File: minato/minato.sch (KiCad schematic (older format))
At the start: 211 parts, among them U1 Elite-C

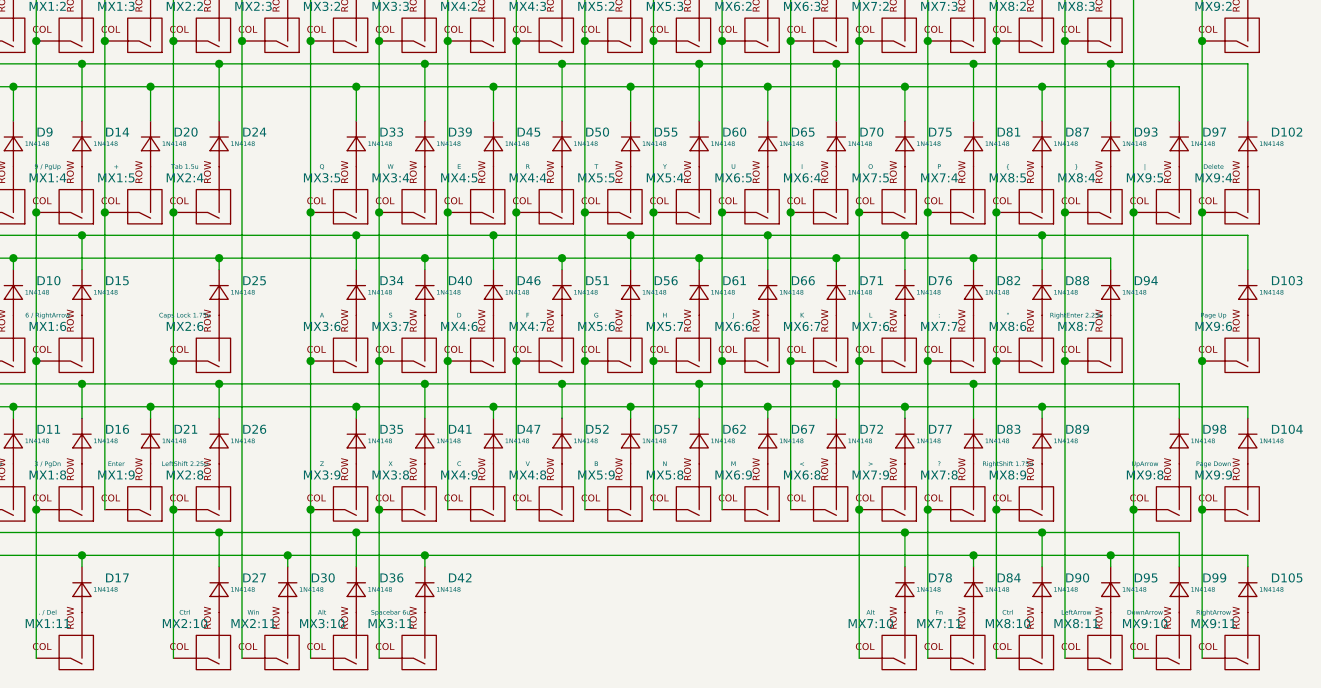
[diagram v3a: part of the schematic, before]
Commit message: :sparkles: Layout basic keyboard switches
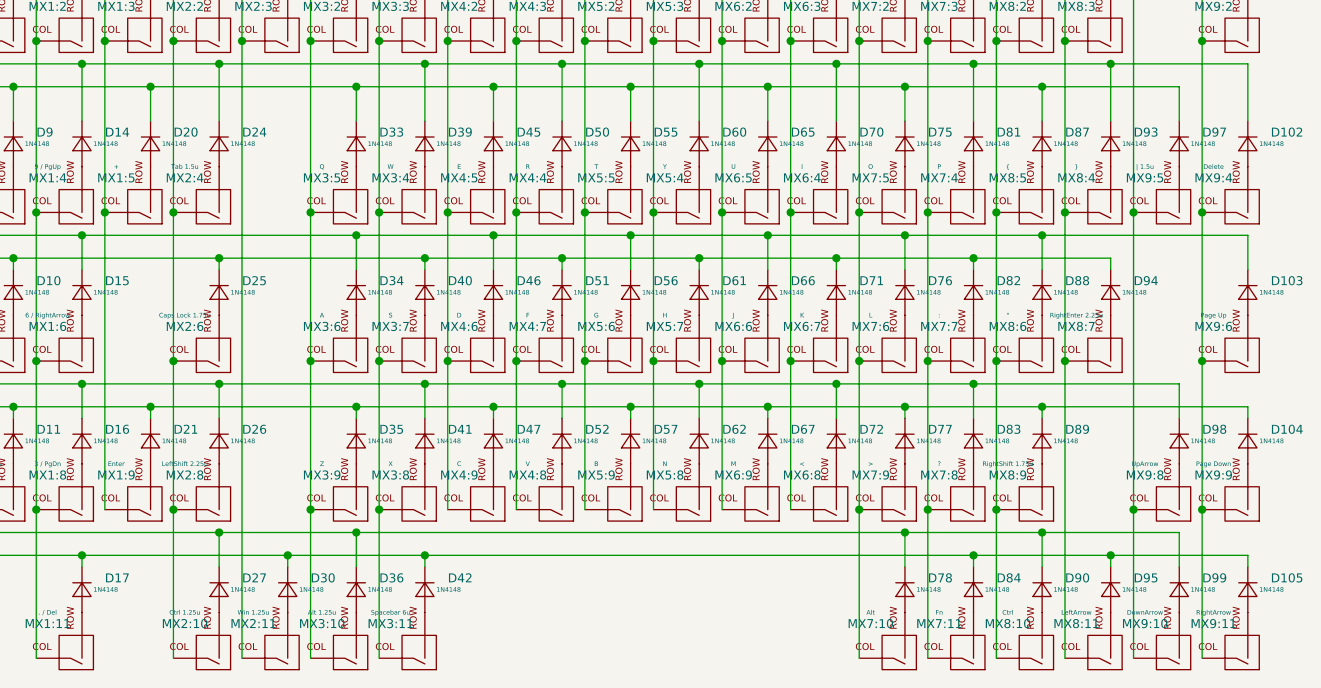
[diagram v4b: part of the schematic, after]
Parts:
- MX2:10: value Ctrl -> Ctrl 1.25u
- MX2:11: value Win -> Win 1.25u
- MX3:10: value Alt -> Alt 1.25u
- MX9:5: value | -> | 1.5u
- U1: footprint Keebio-Parts.pretty:Elite-C -> Keebio-Parts.pretty:Elite-C-castellated-29pin
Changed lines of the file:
@@
 F 0 "U1" H 1550 2337 60  0000 C CNN
 F 1 "Elite-C" H 1550 2231 60  0000 C CNN
-F 2 "Keebio-Parts.pretty:Elite-C" V 2600 -1000 60  0001 C CNN
+F 2 "Keebio-Parts.pretty:Elite-C-castellated-29pin" V 2600 -1000 60  0001 C CNN
 F 3 "" V 2600 -1000 60  0001 C CNN
 	1    1550 1500
@@
 P 9000 3150
 F 0 "MX9:5" H 9100 3050 39  0000 C CNN
-F 1 "|" H 9100 3000 20  0000 C CNN
+F 1 "| 1.5u" H 9100 3000 20  0000 C CNN
 F 2 "keyswitches.pretty:Kailh_socket_MX" H 8375 3125 60  0001 C CNN
 F 3 "" H 8375 3125 60  0001 C CNN
@@
 P 5400 5100
 F 0 "MX3:10" H 5500 5000 39  0000 C CNN
-F 1 "Alt" H 5500 4950 20  0000 C CNN
+F 1 "Alt 1.25u" H 5500 4950 20  0000 C CNN
 F 2 "keyswitches.pretty:Kailh_socket_MX" H 4775 5075 60  0001 C CNN
 F 3 "" H 4775 5075 60  0001 C CNN
@@
 P 5100 5100
 F 0 "MX2:11" H 5200 5000 39  0000 C CNN
-F 1 "Win" H 5200 4950 20  0000 C CNN
+F 1 "Win 1.25u" H 5200 4950 20  0000 C CNN
 F 2 "keyswitches.pretty:Kailh_socket_MX" H 4475 5075 60  0001 C CNN
 F 3 "" H 4475 5075 60  0001 C CNN
@@
 P 4800 5100
 F 0 "MX2:10" H 4900 5000 39  0000 C CNN
-F 1 "Ctrl" H 4900 4950 20  0000 C CNN
+F 1 "Ctrl 1.25u" H 4900 4950 20  0000 C CNN
 F 2 "keyswitches.pretty:Kailh_socket_MX" H 4175 5075 60  0001 C CNN
 F 3 "" H 4175 5075 60  0001 C CNN

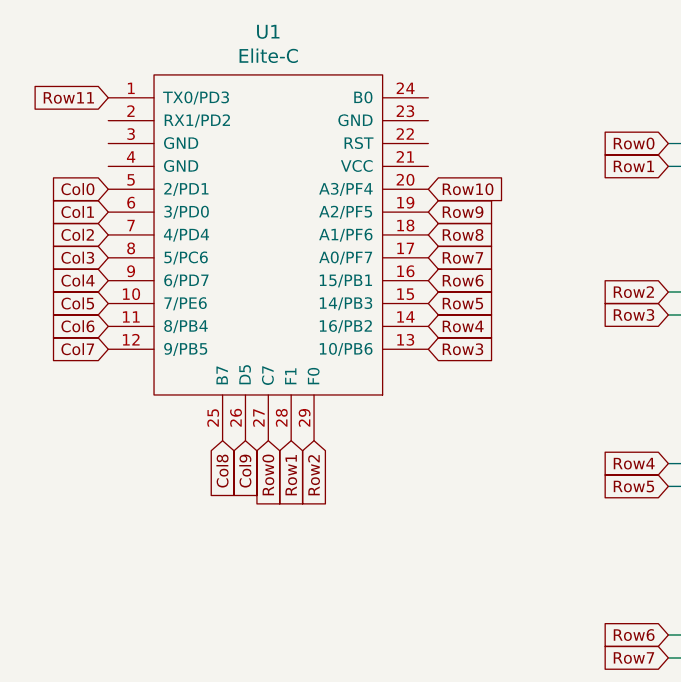
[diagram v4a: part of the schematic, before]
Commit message: :sparkles: Rev. 1 Routing
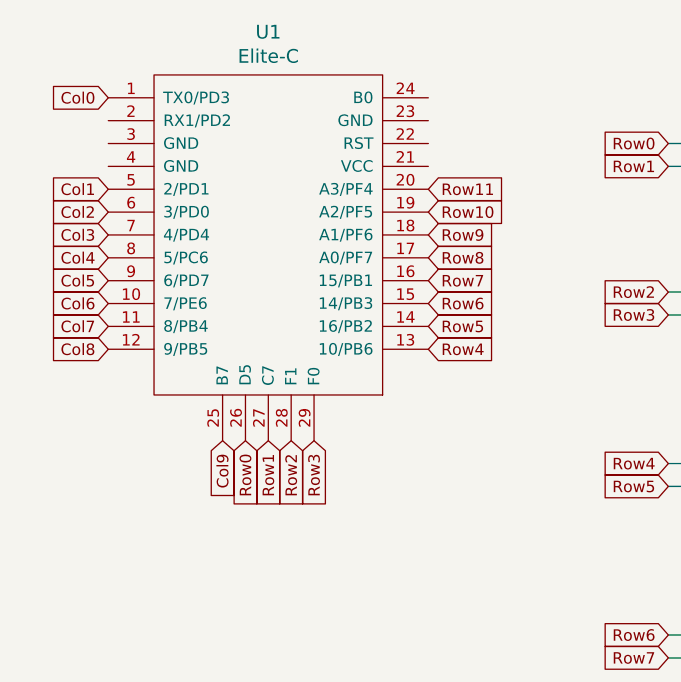
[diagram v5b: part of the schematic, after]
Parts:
- U1: footprint Keebio-Parts.pretty:Elite-C-castellated-29pin -> Keebio-Parts.pretty:Elite-C-castellated-29pin-holes
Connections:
- net Col0: now also U1.1 (TX0/PD3); no longer U1.5 (2/PD1)
- net Col1: now also U1.5 (2/PD1); no longer U1.6 (3/PD0)
- net Col2: now also U1.6 (3/PD0); no longer U1.7 (4/PD4)
- net Col3: now also U1.7 (4/PD4); no longer U1.8 (5/PC6)
- net Col4: now also U1.8 (5/PC6); no longer U1.9 (6/PD7)
- net Col5: now also U1.9 (6/PD7); no longer U1.10 (7/PE6)
- net Col6: now also U1.10 (7/PE6); no longer U1.11 (8/PB4)
- net Col7: now also U1.11 (8/PB4); no longer U1.12 (9/PB5)
- net Col8: now also U1.12 (9/PB5); no longer U1.25 (B7)
- net Col9: now also U1.25 (B7); no longer U1.26 (D5)
- net Row0: now also U1.26 (D5); no longer U1.27 (C7)
- net Row1: now also U1.27 (C7); no longer U1.28 (F1)
- net Row10: now also U1.19 (A2/PF5); no longer U1.20 (A3/PF4)
- net Row11: now also U1.20 (A3/PF4); no longer U1.1 (TX0/PD3)
- net Row2: now also U1.28 (F1); no longer U1.29 (F0)
- net Row3: now also U1.29 (F0); no longer U1.13 (10/PB6)
- net Row4: now also U1.13 (10/PB6); no longer U1.14 (16/PB2)
- net Row5: now also U1.14 (16/PB2); no longer U1.15 (14/PB3)
- net Row6: now also U1.15 (14/PB3); no longer U1.16 (15/PB1)
- net Row7: now also U1.16 (15/PB1); no longer U1.17 (A0/PF7)
- net Row8: now also U1.17 (A0/PF7); no longer U1.18 (A1/PF6)
- net Row9: now also U1.18 (A1/PF6); no longer U1.19 (A2/PF5)
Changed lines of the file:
@@
 EELAYER 30 0
 EELAYER END
-$Descr A0 46811 33110
+$Descr A3 16535 11693
 encoding utf-8
 Sheet 1 1
@@
 F 0 "U1" H 1550 2337 60  0000 C CNN
 F 1 "Elite-C" H 1550 2231 60  0000 C CNN
-F 2 "Keebio-Parts.pretty:Elite-C-castellated-29pin" V 2600 -1000 60  0001 C CNN
+F 2 "Keebio-Parts.pretty:Elite-C-castellated-29pin-holes" V 2600 -1000 60  0001 C CNN
 F 3 "" V 2600 -1000 60  0001 C CNN
 	1    1550 1500
 	1    0    0    -1
 $EndComp
-Text GLabel 850  1350 0    50   Input ~ 0
+Text GLabel 850  950  0    50   Input ~ 0
 Col0
-Text GLabel 850  1450 0    50   Input ~ 0
+Text GLabel 850  1350 0    50   Input ~ 0
 Col1
-Text GLabel 850  1550 0    50   Input ~ 0
+Text GLabel 850  1450 0    50   Input ~ 0
 Col2
-Text GLabel 850  1650 0    50   Input ~ 0
+Text GLabel 850  1550 0    50   Input ~ 0
 Col3
-Text GLabel 850  1750 0    50   Input ~ 0
+Text GLabel 850  1650 0    50   Input ~ 0
 Col4
-Text GLabel 850  1850 0    50   Input ~ 0
+Text GLabel 850  1750 0    50   Input ~ 0
 Col5
-Text GLabel 850  1950 0    50   Input ~ 0
+Text GLabel 850  1850 0    50   Input ~ 0
 Col6
 $Comp
@@
 Wire Wire Line
 	9350 4750 9350 4700
-Text GLabel 850  2050 0    50   Input ~ 0
+Text GLabel 850  1950 0    50   Input ~ 0
 Col7
-Text GLabel 1350 2450 3    50   Input ~ 0
+Text GLabel 850  2050 0    50   Input ~ 0
 Col8
-Text GLabel 1450 2450 3    50   Input ~ 0
+Text GLabel 1350 2450 3    50   Input ~ 0
 Col9
-Text GLabel 1550 2450 3    50   Input ~ 0
+Text GLabel 1450 2450 3    50   Input ~ 0
 Row0
-Text GLabel 1650 2450 3    50   Input ~ 0
+Text GLabel 1550 2450 3    50   Input ~ 0
 Row1
-Text GLabel 1750 2450 3    50   Input ~ 0
+Text GLabel 1650 2450 3    50   Input ~ 0
 Row2
-Text GLabel 2250 2050 2    50   Input ~ 0
+Text GLabel 1750 2450 3    50   Input ~ 0
 Row3
-Text GLabel 2250 1950 2    50   Input ~ 0
+Text GLabel 2250 2050 2    50   Input ~ 0
 Row4
-Text GLabel 2250 1850 2    50   Input ~ 0
+Text GLabel 2250 1950 2    50   Input ~ 0
 Row5
-Text GLabel 2250 1750 2    50   Input ~ 0
+Text GLabel 2250 1850 2    50   Input ~ 0
 Row6
-Text GLabel 2250 1650 2    50   Input ~ 0
+Text GLabel 2250 1750 2    50   Input ~ 0
 Row7
-Text GLabel 2250 1550 2    50   Input ~ 0
+Text GLabel 2250 1650 2    50   Input ~ 0
 Row8
-Text GLabel 2250 1450 2    50   Input ~ 0
+Text GLabel 2250 1550 2    50   Input ~ 0
 Row9
-Text GLabel 2250 1350 2    50   Input ~ 0
+Text GLabel 2250 1450 2    50   Input ~ 0
 Row10
-Text GLabel 850  950  0    50   Input ~ 0
+Text GLabel 2250 1350 2    50   Input ~ 0
 Row11
 $Comp

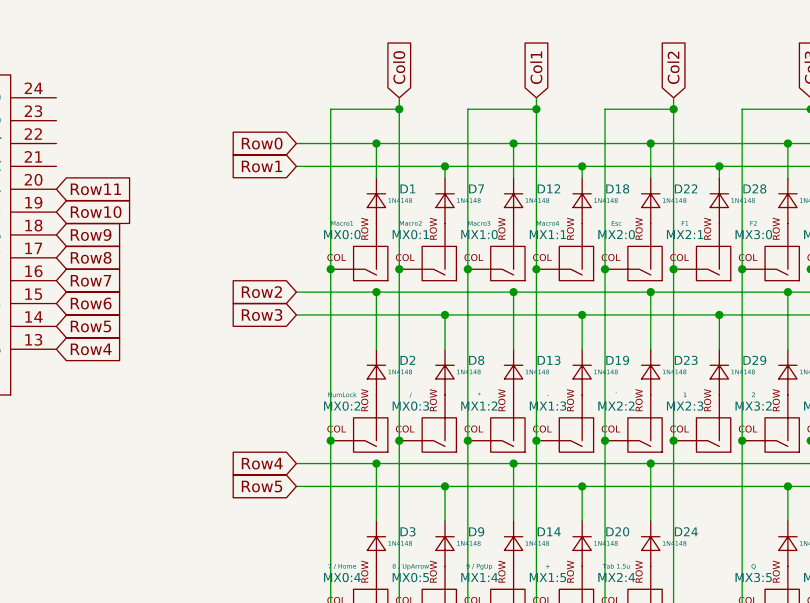
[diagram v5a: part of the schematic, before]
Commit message: :sparkles: Rev. 2 Routing
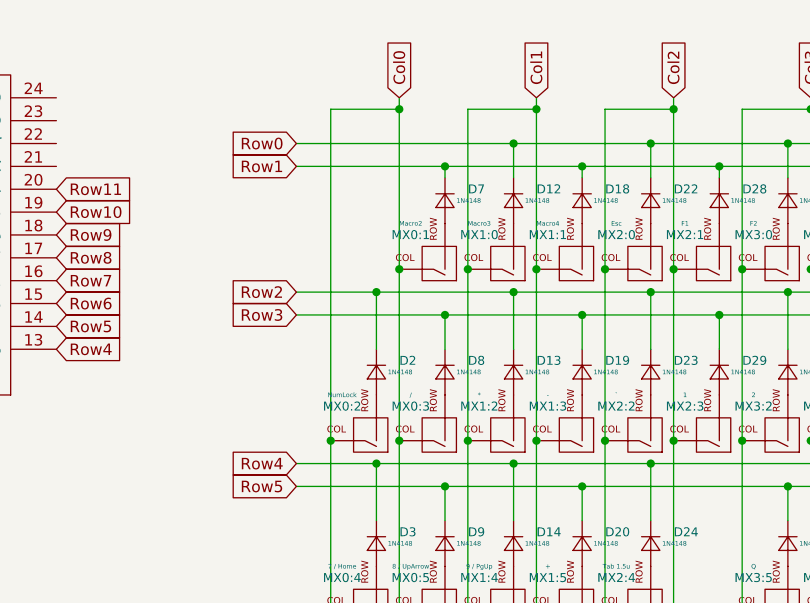
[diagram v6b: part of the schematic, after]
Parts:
- removed D1: 1N4148, Diode_SMD:D_SOD-123, symbol Device:D_Small
- removed MX0:0: Macro1, keyswitches.pretty:Kailh_socket_MX, symbol MX_Alps_Hybrid:MX-NoLED
- U1: footprint Keebio-Parts.pretty:Elite-C-castellated-29pin-holes -> Keebio-Parts.pretty:Elite-C-castellated-29pin
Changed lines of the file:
@@
 F 0 "U1" H 1550 2337 60  0000 C CNN
 F 1 "Elite-C" H 1550 2231 60  0000 C CNN
-F 2 "Keebio-Parts.pretty:Elite-C-castellated-29pin-holes" V 2600 -1000 60  0001 C CNN
+F 2 "Keebio-Parts.pretty:Elite-C-castellated-29pin" V 2600 -1000 60  0001 C CNN
 F 3 "" V 2600 -1000 60  0001 C CNN
 	1    1550 1500
@@
 Text GLabel 850  1850 0    50   Input ~ 0
 Col6
-$Comp
-L Device:D_Small D1
-U 1 1 5E820E4A
-P 3650 1400
-F 0 "D1" V 3600 1500 39  0000 L CNN
-F 1 "1N4148" V 3650 1450 20  0000 L CNN
-F 2 "Diode_SMD:D_SOD-123" V 3650 1400 50  0001 C CNN
-F 3 "~" V 3650 1400 50  0001 C CNN
-	1    3650 1400
-	0    1    1    0
-$EndComp
 Text GLabel 3300 1250 0    50   Input ~ 0
 Row1
@@
 Col0
 $Comp
-L Device:D_Small D7
-U 1 1 5E820E58
-P 3950 1400
-F 0 "D7" V 3900 1500 39  0000 L CNN
-F 1 "1N4148" V 3950 1450 20  0000 L CNN
-F 2 "Diode_SMD:D_SOD-123" V 3950 1400 50  0001 C CNN
-F 3 "~" V 3950 1400 50  0001 C CNN
-	1    3950 1400
-	0    1    1    0
-$EndComp
-$Comp
-L MX_Alps_Hybrid:MX-NoLED MX0:1
-U 1 1 5E820E5E
-P 3900 1650
-F 0 "MX0:1" H 4000 1550 39  0000 C CNN
-F 1 "Macro2" H 4000 1500 20  0000 C CNN
-F 2 "keyswitches.pretty:Kailh_socket_MX" H 3275 1625 60  0001 C CNN
-F 3 "" H 3275 1625 60  0001 C CNN
-	1    3900 1650
-	-1   0    0    1
-$EndComp
-$Comp
-L Device:D_Small D12
-U 1 1 5E820E64
-P 4250 1400
-F 0 "D12" V 4200 1500 39  0000 L CNN
-F 1 "1N4148" V 4250 1450 20  0000 L CNN
-F 2 "Diode_SMD:D_SOD-123" V 4250 1400 50  0001 C CNN
-F 3 "~" V 4250 1400 50  0001 C CNN
-	1    4250 1400
-	0    1    1    0
-$EndComp
-$Comp
-L MX_Alps_Hybrid:MX-NoLED MX1:0
-U 1 1 5E820E6A
-P 4200 1650
-F 0 "MX1:0" H 4300 1550 39  0000 C CNN
-F 1 "Macro3" H 4300 1500 20  0000 C CNN
-F 2 "keyswitches.pretty:Kailh_socket_MX" H 3575 1625 60  0001 C CNN
-F 3 "" H 3575 1625 60  0001 C CNN
-	1    4200 1650
-	-1   0    0    1
-$EndComp
-$Comp
-L Device:D_Small D18
-U 1 1 5E820E70
-P 4550 1400
-F 0 "D18" V 4500 1500 39  0000 L CNN
-F 1 "1N4148" V 4550 1450 20  0000 L CNN
-F 2 "Diode_SMD:D_SOD-123" V 4550 1400 50  0001 C CNN
-F 3 "~" V 4550 1400 50  0001 C CNN
-	1    4550 1400
-	0    1    1    0
-$EndComp
-$Comp
-L MX_Alps_Hybrid:MX-NoLED MX1:1
-U 1 1 5E820E76
-P 4500 1650
-F 0 "MX1:1" H 4600 1550 39  0000 C CNN
-F 1 "Macro4" H 4600 1500 20  0000 C CNN
-F 2 "keyswitches.pretty:Kailh_socket_MX" H 3875 1625 60  0001 C CNN
-F 3 "" H 3875 1625 60  0001 C CNN
-	1    4500 1650
-	-1   0    0    1
-$EndComp
-$Comp
 L Device:D_Small D2
 U 1 1 5E820E7C
@@
 Col9
 $Comp
-L MX_Alps_Hybrid:MX-NoLED MX0:0
-U 1 1 5E820E51
-P 3600 1650
-F 0 "MX0:0" H 3700 1550 39  0000 C CNN
-F 1 "Macro1" H 3700 1500 20  0000 C CNN
-F 2 "keyswitches.pretty:Kailh_socket_MX" H 2975 1625 60  0001 C CNN
-F 3 "" H 2975 1625 60  0001 C CNN
-	1    3600 1650
-	-1   0    0    1
-$EndComp
-$Comp
 L MX_Alps_Hybrid:MX-NoLED MX9:11
 U 1 1 5E821384
@@
 Text GLabel 3300 4700 0    50   Input ~ 0
 Row11
-Wire Wire Line
-	3300 1250 3950 1250
-Wire Wire Line
-	3300 1150 3650 1150
 $Comp
 L MX_Alps_Hybrid:MX-NoLED MX9:6
@@
 	3300 4700 4250 4700
 Wire Wire Line
-	3750 1700 3750 1000
-Wire Wire Line
-	3450 1700 3450 1000
-Wire Wire Line
 	3450 1000 3750 1000
 Connection ~ 3750 1000
 Wire Wire Line
 	3750 1000 3750 950
-Wire Wire Line
-	3750 1700 3750 2450
-Connection ~ 3750 1700
 Connection ~ 3750 2450
 Wire Wire Line
@@
 Wire Wire Line
 	3450 5150 3450 4500
-Connection ~ 3450 1700
 Connection ~ 3450 2450
-Wire Wire Line
-	3450 2450 3450 1700
 Connection ~ 3450 3200
 Wire Wire Line
@@
 Wire Wire Line
 	4350 950  4350 1000
-Connection ~ 4350 1700
-Wire Wire Line
-	4350 1700 4350 2450
 Connection ~ 4350 2450
 Wire Wire Line
@@
 Wire Wire Line
 	4350 1000 4050 1000
-Wire Wire Line
-	4050 1000 4050 1700
 Connection ~ 4350 1000
-Wire Wire Line
-	4350 1000 4350 1700
-Connection ~ 4050 1700
-Wire Wire Line
-	4050 1700 4050 2450
 Connection ~ 4050 2450
 Wire Wire Line
@@
 	8850 4500 8850 5150
 Wire Wire Line
-	3650 1300 3650 1150
-Connection ~ 3650 1150
-Wire Wire Line
-	3650 1150 4250 1150
-Wire Wire Line
-	3950 1300 3950 1250
-Connection ~ 3950 1250
-Wire Wire Line
-	3950 1250 4550 1250
-Wire Wire Line
-	4250 1300 4250 1150
-Connection ~ 4250 1150
-Wire Wire Line
-	4250 1150 4850 1150
-Wire Wire Line
-	4550 1300 4550 1250
-Connection ~ 4550 1250
-Wire Wire Line
-	4550 1250 5150 1250
-Wire Wire Line
 	4850 1300 4850 1150
 Connection ~ 4850 1150
@@
 	-1   0    0    1
 $EndComp
+Wire Wire Line
+	4550 1250 5150 1250
+Connection ~ 4550 1250
+Wire Wire Line
+	4550 1300 4550 1250
+$Comp
+L Device:D_Small D18
+U 1 1 5E820E70
+P 4550 1400
+F 0 "D18" V 4500 1500 39  0000 L CNN
+F 1 "1N4148" V 4550 1450 20  0000 L CNN
+F 2 "Diode_SMD:D_SOD-123" V 4550 1400 50  0001 C CNN
+F 3 "~" V 4550 1400 50  0001 C CNN
+	1    4550 1400
+	0    1    1    0
+$EndComp
+Wire Wire Line
+	4350 1000 4350 1700
+Wire Wire Line
+	4350 1700 4350 2450
+Connection ~ 4350 1700
+$Comp
+L MX_Alps_Hybrid:MX-NoLED MX1:1
+U 1 1 5E820E76
+P 4500 1650
+F 0 "MX1:1" H 4600 1550 39  0000 C CNN
+F 1 "Macro4" H 4600 1500 20  0000 C CNN
+F 2 "keyswitches.pretty:Kailh_socket_MX" H 3875 1625 60  0001 C CNN
+F 3 "" H 3875 1625 60  0001 C CNN
+	1    4500 1650
+	-1   0    0    1
+$EndComp
+Wire Wire Line
+	4250 1150 4850 1150
+Connection ~ 4250 1150
+Wire Wire Line
+	4250 1300 4250 1150
+$Comp
+L Device:D_Small D12
+U 1 1 5E820E64
+P 4250 1400
+F 0 "D12" V 4200 1500 39  0000 L CNN
+F 1 "1N4148" V 4250 1450 20  0000 L CNN
+F 2 "Diode_SMD:D_SOD-123" V 4250 1400 50  0001 C CNN
+F 3 "~" V 4250 1400 50  0001 C CNN
+	1    4250 1400
+	0    1    1    0
+$EndComp
+Wire Wire Line
+	4050 1700 4050 2450
+Wire Wire Line
+	4050 1000 4050 1700
+Connection ~ 4050 1700
+$Comp
+L MX_Alps_Hybrid:MX-NoLED MX1:0
+U 1 1 5E820E6A
+P 4200 1650
+F 0 "MX1:0" H 4300 1550 39  0000 C CNN
+F 1 "Macro3" H 4300 1500 20  0000 C CNN
+F 2 "keyswitches.pretty:Kailh_socket_MX" H 3575 1625 60  0001 C CNN
+F 3 "" H 3575 1625 60  0001 C CNN
+	1    4200 1650
+	-1   0    0    1
+$EndComp
+Wire Wire Line
+	3950 1250 4550 1250
+Wire Wire Line
+	3300 1250 3950 1250
+Connection ~ 3950 1250
+Wire Wire Line
+	3950 1300 3950 1250
+$Comp
+L Device:D_Small D7
+U 1 1 5E820E58
+P 3950 1400
+F 0 "D7" V 3900 1500 39  0000 L CNN
+F 1 "1N4148" V 3950 1450 20  0000 L CNN
+F 2 "Diode_SMD:D_SOD-123" V 3950 1400 50  0001 C CNN
+F 3 "~" V 3950 1400 50  0001 C CNN
+	1    3950 1400
+	0    1    1    0
+$EndComp
+Wire Wire Line
+	3750 1700 3750 2450
+Wire Wire Line
+	3750 1700 3750 1000
+Connection ~ 3750 1700
+$Comp
+L MX_Alps_Hybrid:MX-NoLED MX0:1
+U 1 1 5E820E5E
+P 3900 1650
+F 0 "MX0:1" H 4000 1550 39  0000 C CNN
+F 1 "Macro2" H 4000 1500 20  0000 C CNN
+F 2 "keyswitches.pretty:Kailh_socket_MX" H 3275 1625 60  0001 C CNN
+F 3 "" H 3275 1625 60  0001 C CNN
+	1    3900 1650
+	-1   0    0    1
+$EndComp
+Wire Wire Line
+	3450 1000 3450 2450
+Wire Wire Line
+	3300 1150 4250 1150
 $EndSCHEMATC

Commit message: :tada: Rev 1 initial design complete
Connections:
- net GND: now reaches U1.23 (GND)
- net GND: now also U1.3 (GND), U1.4 (GND)
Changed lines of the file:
@@
 Wire Wire Line
 	3300 1150 4250 1150
+$Comp
+L power:GND #PWR?
+U 1 1 5E57B2BC
+P 850 1250
+F 0 "#PWR?" H 850 1000 50  0001 C CNN
+F 1 "GND" V 855 1122 50  0000 R CNN
+F 2 "" H 850 1250 50  0001 C CNN
+F 3 "" H 850 1250 50  0001 C CNN
+	1    850  1250
+	0    1    1    0
+$EndComp
+$Comp
+L power:GND #PWR?
+U 1 1 5E57CB9D
+P 2250 1050
+F 0 "#PWR?" H 2250 800 50  0001 C CNN
+F 1 "GND" V 2255 922 50  0000 R CNN
+F 2 "" H 2250 1050 50  0001 C CNN
+F 3 "" H 2250 1050 50  0001 C CNN
+	1    2250 1050
+	0    -1   -1   0
+$EndComp
+$Comp
+L power:GND #PWR?
+U 1 1 5E57DFD0
+P 850 1150
+F 0 "#PWR?" H 850 900 50  0001 C CNN
+F 1 "GND" V 855 1022 50  0000 R CNN
+F 2 "" H 850 1150 50  0001 C CNN
+F 3 "" H 850 1150 50  0001 C CNN
+	1    850  1150
+	0    1    1    0
+$EndComp
 $EndSCHEMATC
